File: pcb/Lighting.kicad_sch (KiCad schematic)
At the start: 5 parts, among them U4 TXS0101DBV

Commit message: First pass of applying footprints to most components.
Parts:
- JP10: footprint (none) -> Jumper:SolderJumper-2_P1.3mm_Bridged_RoundedPad1.0x1.5mm
- JP11: footprint (none) -> Jumper:SolderJumper-2_P1.3mm_Open_TrianglePad1.0x1.5mm
- R8: footprint (none) -> Resistor_SMD:R_0603_1608Metric_Pad0.98x0.95mm_HandSolder
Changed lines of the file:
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@@
 			)
 		)
-		(property "Footprint" ""
+		(property "Footprint" "Jumper:SolderJumper-2_P1.3mm_Open_TrianglePad1.0x1.5mm"
 			(at 101.6 49.53 0)
 			(effects
@@
 			)
 		)
-		(property "Footprint" ""
+		(property "Footprint" "Jumper:SolderJumper-2_P1.3mm_Bridged_RoundedPad1.0x1.5mm"
 			(at 88.9 77.47 0)
 			(effects
@@
 			)
 		)
-		(property "Footprint" ""
+		(property "Footprint" "Resistor_SMD:R_0603_1608Metric_Pad0.98x0.95mm_HandSolder"
 			(at 88.9 47.752 90)
 			(effects

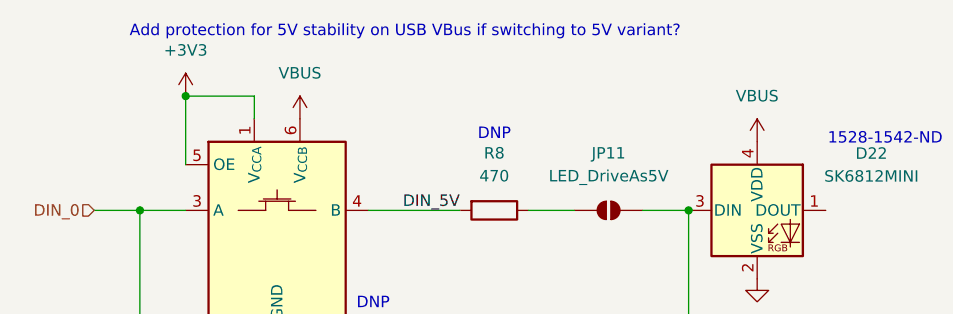
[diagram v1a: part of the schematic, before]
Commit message: Switching from a full USB protection chip for OVP and ESD, needed for USB PD to only ESD protection. Also added chips for ESD protection for the Ethernet connectors to the other hand.
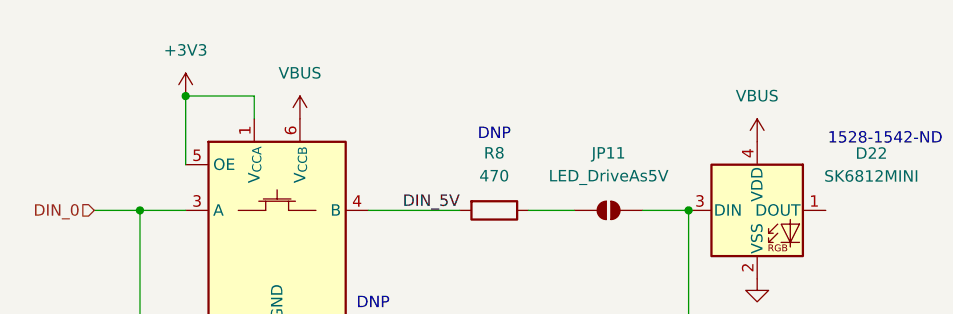
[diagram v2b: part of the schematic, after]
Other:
- note removed: "Add protection for 5V stability on USB VBus if switching to 5V variant?"
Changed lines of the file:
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@@
-		)
-	)
-	(text "Add protection for 5V stability on USB VBus if switching to 5V variant?"
-		(exclude_from_sim no)
-		(at 78.994 29.718 0)
-		(effects
-			(font
-				(size 1.27 1.27)
-			)
 		)
 	)

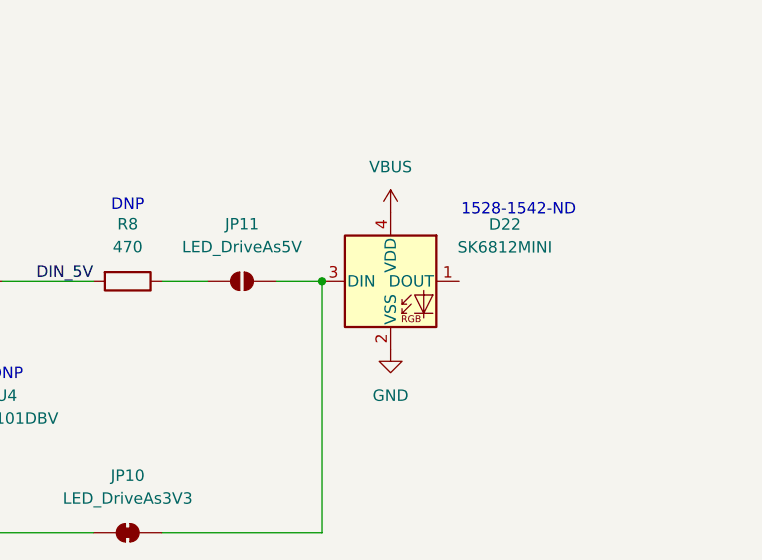
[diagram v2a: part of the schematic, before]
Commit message: Adding jumpers to test/swap between powering SK6812 with 3.3V or 5V.
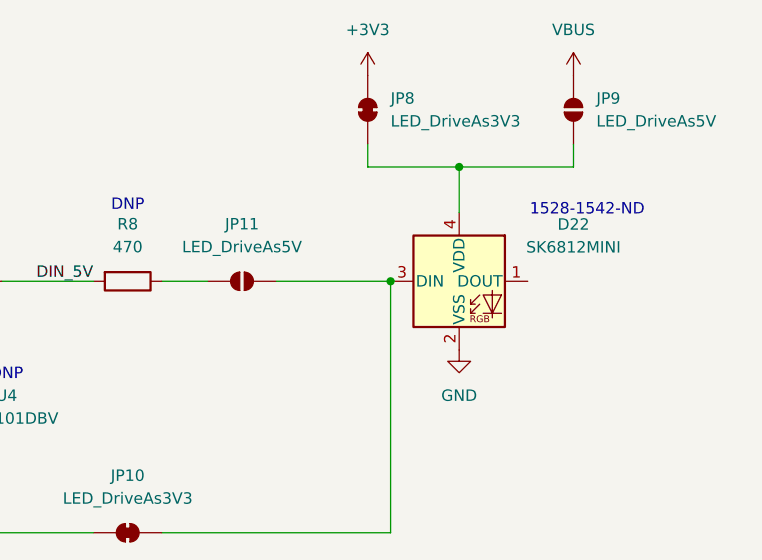
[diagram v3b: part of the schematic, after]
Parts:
- added JP8: LED_DriveAs3V3, Jumper:SolderJumper-2_P1.3mm_Bridged_RoundedPad1.0x1.5mm, symbol Jumper:SolderJumper_2_Bridged
- added JP9: LED_DriveAs5V, Jumper:SolderJumper-2_P1.3mm_Open_TrianglePad1.0x1.5mm, symbol Jumper:SolderJumper_2_Open
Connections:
- net +3V3: now also JP8.2 (B)
- net VBUS: now also JP9.2 (B); no longer D22.4 (VDD)
- new net: D22.4 (VDD), JP8.1 (A), JP9.1 (A)
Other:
- moved on the sheet: D22

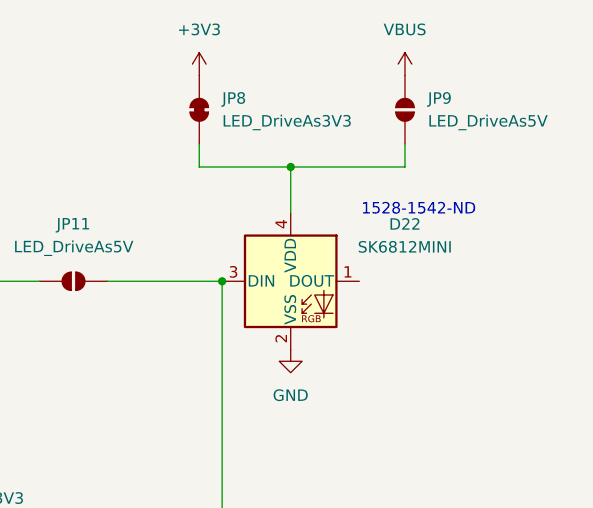
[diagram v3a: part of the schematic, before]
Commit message: Starting to position components and flipping passives as needed. Looking like board size is likely to need to be expanded.
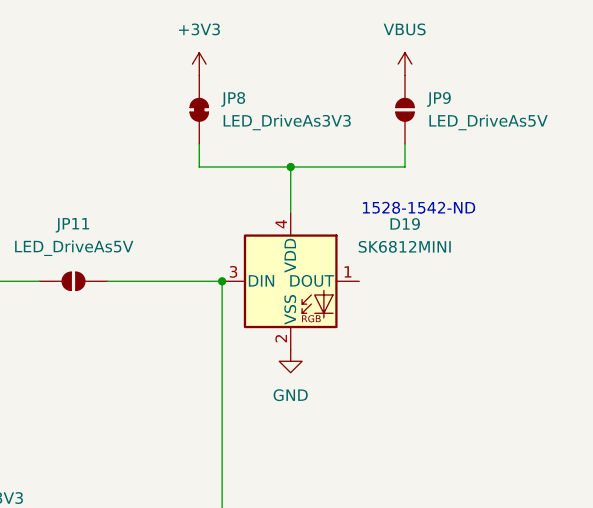
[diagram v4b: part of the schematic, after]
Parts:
- renumbered D22 to D19
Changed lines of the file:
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@@
 		(dnp no)
 		(fields_autoplaced yes)
-		(property "Reference" "D22"
+		(property "Reference" "D19"
 			(at 138.43 43.2114 0)
 			(effects
@@
 			(project "cheapino"
 				(path "/9203b006-47ac-4f34-8cc4-2b709e3df56f/23d46689-c88a-4d8a-9ead-5dd5573c8b8b"
-					(reference "D22")
+					(reference "D19")
 					(unit 1)
 				)

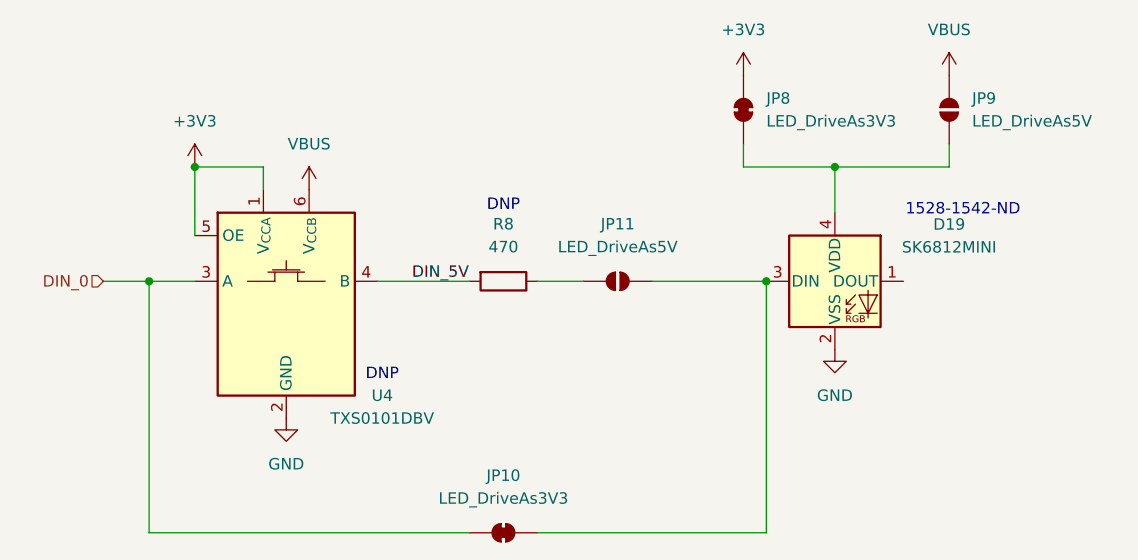
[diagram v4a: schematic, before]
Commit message: WIP: Starting to migrate toward 2 independant halves.
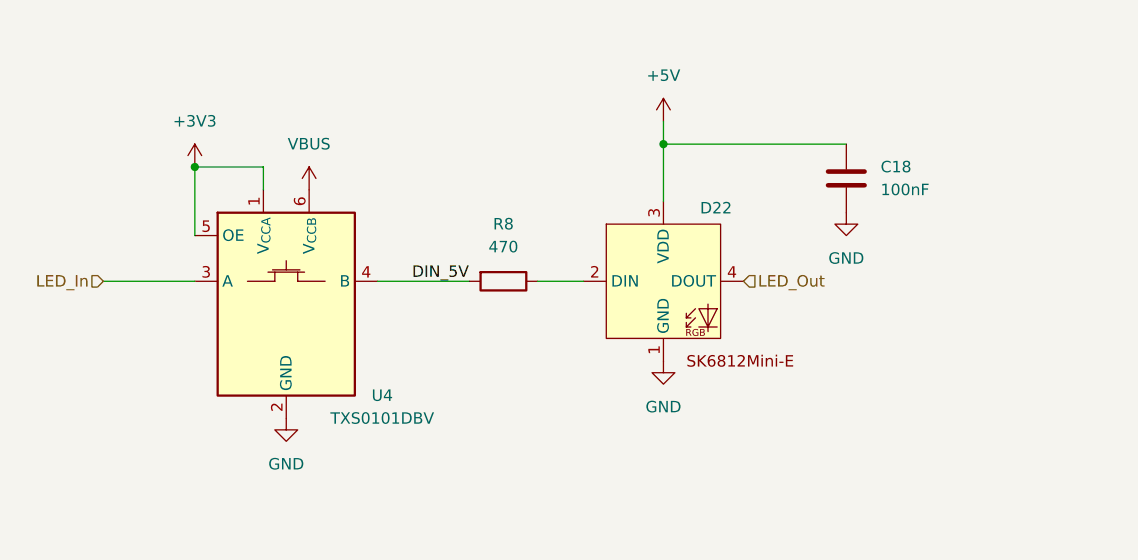
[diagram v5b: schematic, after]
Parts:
- removed D19: SK6812MINI, LED_SMD:LED_SK6812MINI_PLCC4_3.5x3.5mm_P1.75mm, symbol LED:SK6812MINI
- removed JP10, JP8: LED_DriveAs3V3, Jumper:SolderJumper-2_P1.3mm_Bridged_RoundedPad1.0x1.5mm, symbol Jumper:SolderJumper_2_Bridged
- removed JP11, JP9: LED_DriveAs5V, Jumper:SolderJumper-2_P1.3mm_Open_TrianglePad1.0x1.5mm, symbol Jumper:SolderJumper_2_Open
- added C18: 100nF, Capacitor_SMD:C_0805_2012Metric_Pad1.18x1.45mm_HandSolder, symbol Device:C
- added D22: ~, Extra:SK6812-MINI-E_ReverseMount, symbol Extra:SK6812Mini-E
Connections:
- net GND: now also C18.2, D22.1 (GND)
- net at R8.1: now also D22.2 (DIN)
- net DIN_0 renamed LED_In
- new net +5V: C18.1, D22.3 (VDD)
- new net LED_Out: D22.4 (DOUT)
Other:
- note removed: "1528-1542-ND"
- note removed: "DNP"

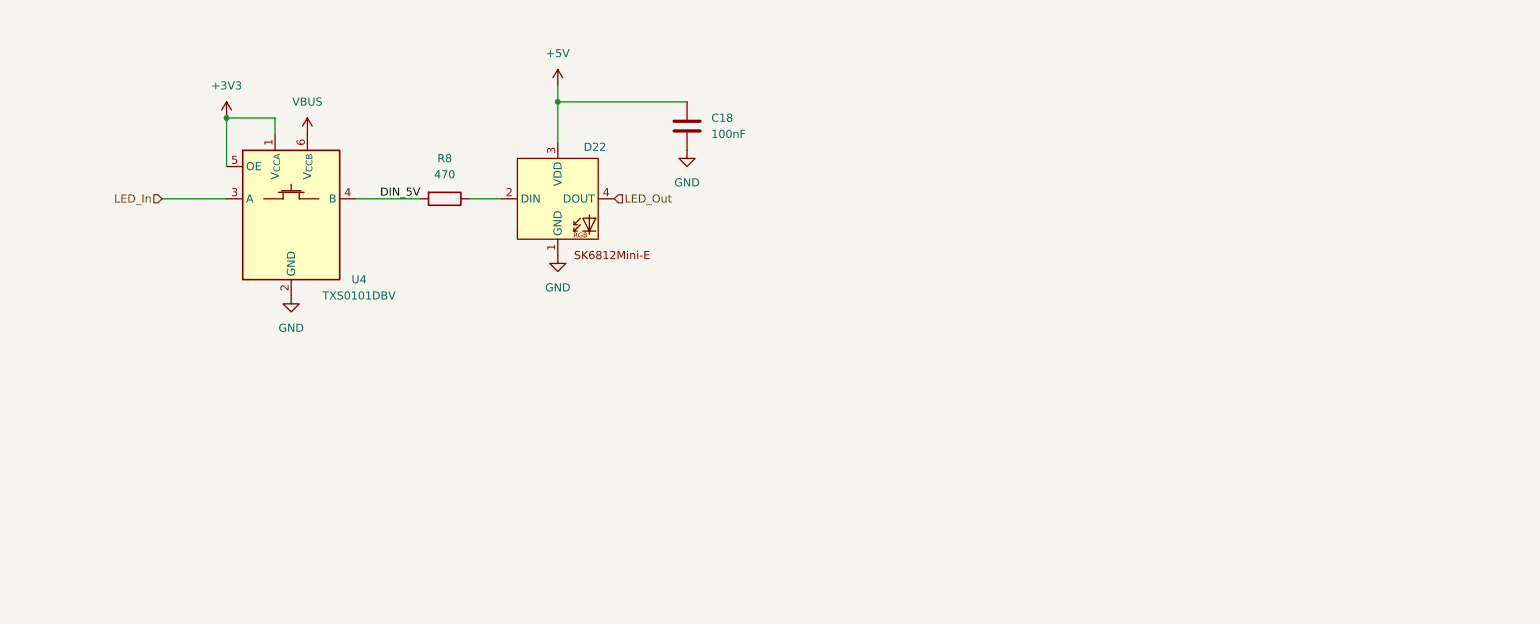
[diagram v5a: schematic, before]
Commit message: WIP: Updating keyboard matrix to use the new shared part and reorganizing all the LED outputs.
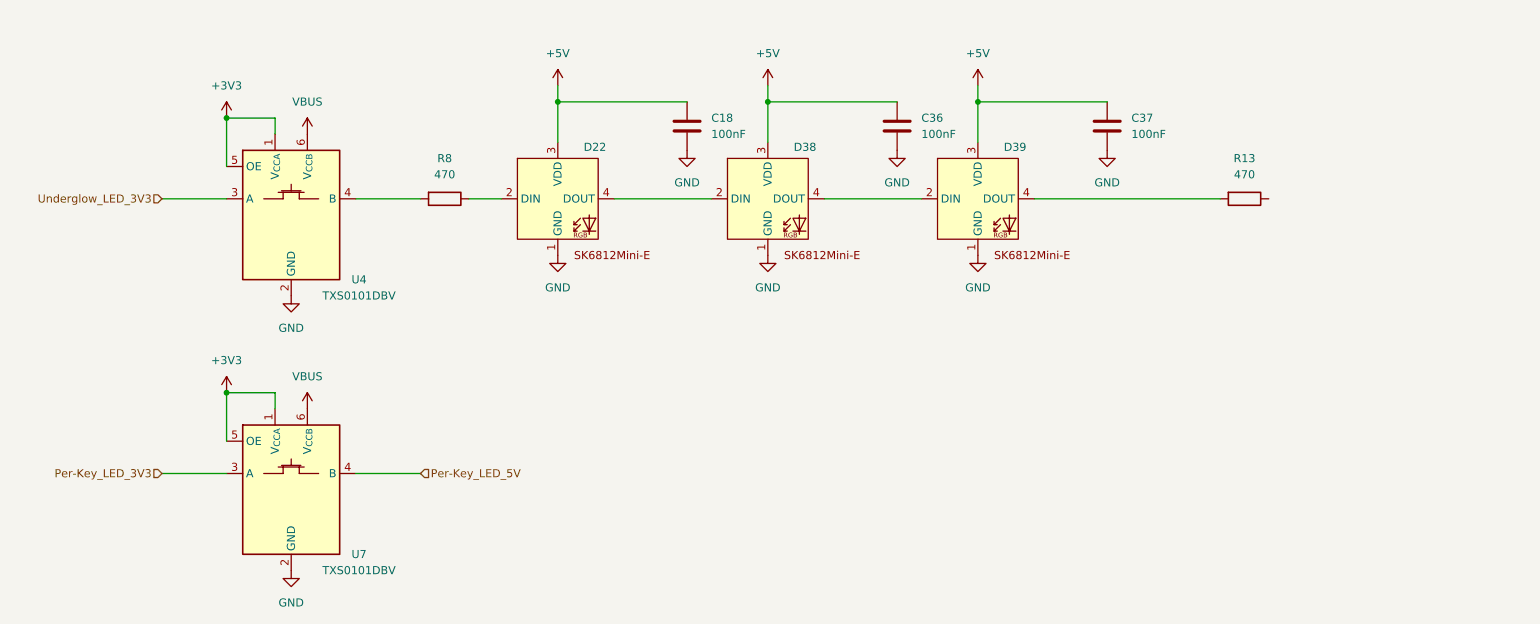
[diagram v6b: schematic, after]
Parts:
- added C36, C37: 100nF, Capacitor_SMD:C_0603_1608Metric_Pad1.08x0.95mm_HandSolder, symbol Device:C
- added D38, D39: ~, Extra:SK6812-MINI-E_ReverseMount, symbol Extra:SK6812Mini-E
- added R13: 470, Resistor_SMD:R_0603_1608Metric_Pad0.98x0.95mm_HandSolder, symbol Device:R
- added U7: TXS0101DBV, Package_TO_SOT_SMD:SOT-23-6, symbol Logic_LevelTranslator:TXS0101DBV
- C18: footprint Capacitor_SMD:C_0805_2012Metric_Pad1.18x1.45mm_HandSolder -> Capacitor_SMD:C_0603_1608Metric_Pad1.08x0.95mm_HandSolder
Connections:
- net +3V3: now also U7.1 (V_{CCA}), U7.5 (OE)
- net +5V: now also C36.1, C37.1, D38.3 (VDD), D39.3 (VDD)
- net GND: now also C36.2, C37.2, D38.1 (GND), D39.1 (GND), U7.2 (GND)
- net VBUS: now also U7.6 (V_{CCB})
- net DIN_5V: no longer names the net of R8.2, U4.4 (B)
- net LED_In renamed Underglow_LED_3V3
- net LED_Out: no longer names the net of D22.4 (DOUT)
- net LED_Out: now also D38.2 (DIN)
- new net: D39.4 (DOUT), R13.2
- new net: D38.4 (DOUT), D39.2 (DIN)
- new net Per-Key_LED_3V3: U7.3 (A)
- new net Per-Key_LED_5V: U7.4 (B)

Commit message: Adding reversible MX Sockets and SK6812MiniE footprints, finishing the replacement of Ethernet with a TRRS connector and selectable 0Ohm resistors to swap Rx/Tx for the interconnect.
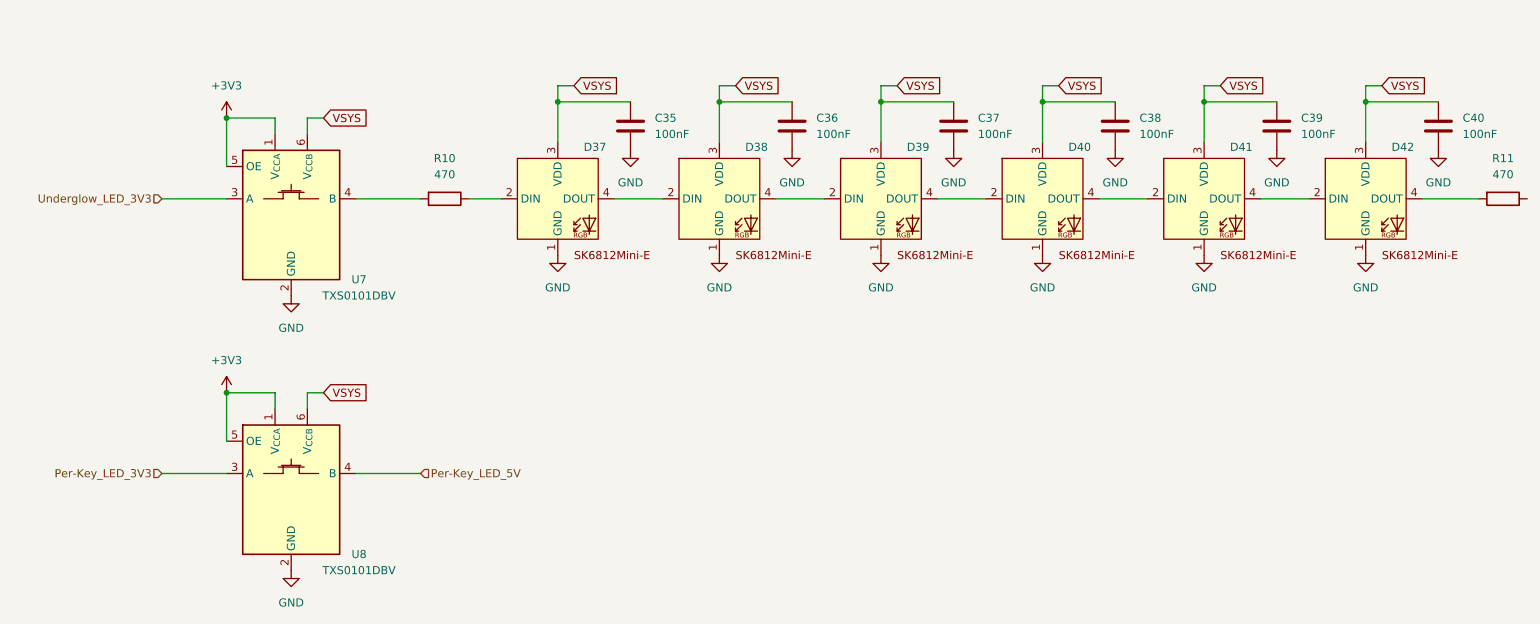
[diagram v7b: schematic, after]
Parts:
- added C38, C39, C40: 100nF, Capacitor_SMD:C_0603_1608Metric_Pad1.08x0.95mm_HandSolder, symbol Device:C
- added D40, D41, D42: ~, Extra:SK6812-MINI-E_ReverseMount_reversible, symbol Extra:SK6812Mini-E
- D37: renamed from D22; footprint Extra:SK6812-MINI-E_ReverseMount -> Extra:SK6812-MINI-E_ReverseMount_reversible
- D38, D39: footprint Extra:SK6812-MINI-E_ReverseMount -> Extra:SK6812-MINI-E_ReverseMount_reversible
- R10: renamed from R8; footprint Resistor_SMD:R_0603_1608Metric_Pad0.98x0.95mm_HandSolder -> Resistor_SMD:R_0805_2012Metric_Pad1.20x1.40mm_HandSolder
- R11: renamed from R13; footprint Resistor_SMD:R_0603_1608Metric_Pad0.98x0.95mm_HandSolder -> Resistor_SMD:R_0805_2012Metric_Pad1.20x1.40mm_HandSolder
- renumbered C18 to C35, U4 to U7, U7 to U8
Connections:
- net VBUS is gone; now on net VSYS: U7.6 (V_{CCB}), U8.6 (V_{CCB})
- net GND: now also C38.2, C39.2, C40.2, D40.1 (GND), D41.1 (GND), D42.1 (GND)
- net at D39.4 (DOUT): now also D40.2 (DIN); no longer R11.2
- net +5V renamed VSYS
- net VSYS: now also C38.1, C39.1, C40.1, D40.3 (VDD), D41.3 (VDD), D42.3 (VDD)
- new net: D40.4 (DOUT), D41.2 (DIN)
- new net: D42.4 (DOUT), R11.2
- new net: D41.4 (DOUT), D42.2 (DIN)
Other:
- moved on the sheet: C35, C36, C37, D38, D39, R11

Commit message: Broke out Underglow LEDs into a common hierarchical sheet for what may be more consistent placements. Additionally created hierarchical PCB layouts and started using the HierarchicalPcb plugin (https://github.com/gauravmm/HierarchicalPcb.git) to automatically layout repeated components for the keymap.
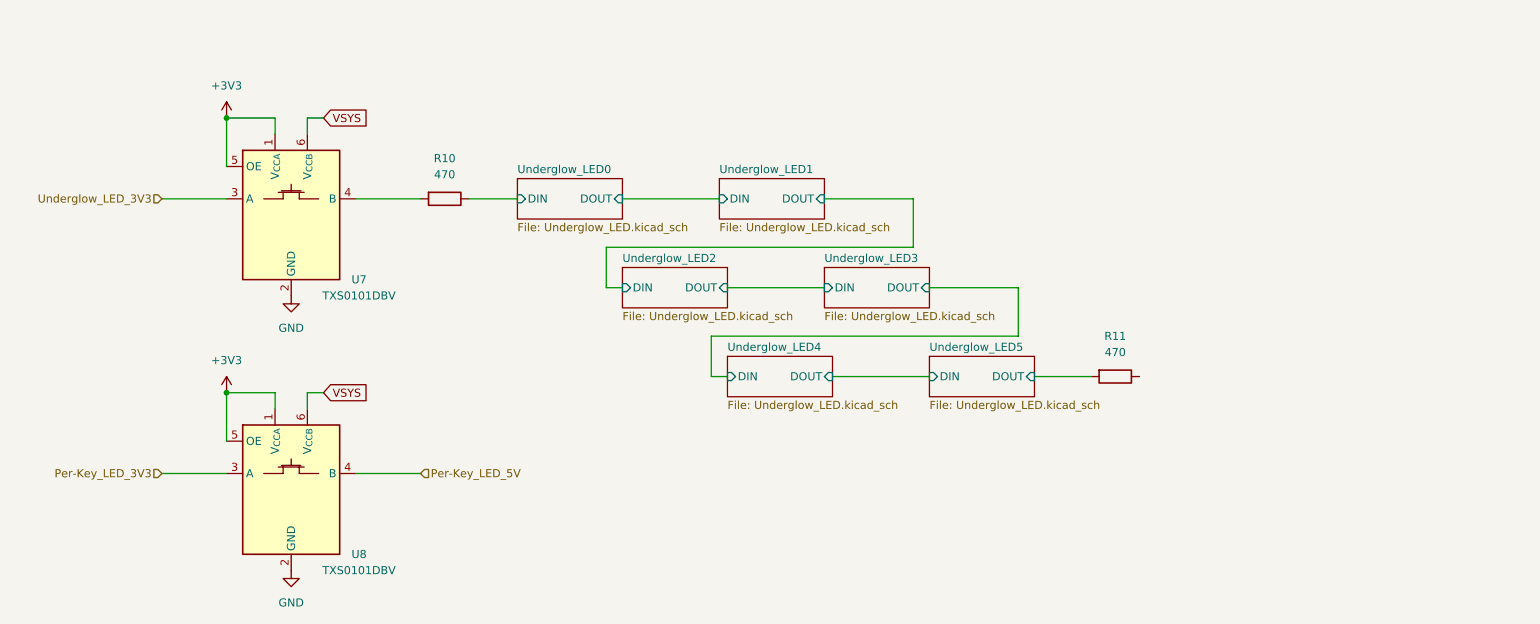
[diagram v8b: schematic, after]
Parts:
- removed C35, C36, C37, C38, C39, C40: 100nF, Capacitor_SMD:C_0603_1608Metric_Pad1.08x0.95mm_HandSolder, symbol Device:C
- removed D37, D38, D39, D40, D41, D42: ~, Extra:SK6812-MINI-E_ReverseMount_reversible, symbol Extra:SK6812Mini-E
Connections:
- net Underglow_LED0/DIN: now reaches R10.1
- net Underglow_LED5/DOUT: now reaches R11.2
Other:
- added sheet Underglow_LED0 (Underglow_LED.kicad_sch)
- added sheet Underglow_LED1 (Underglow_LED.kicad_sch)
- added sheet Underglow_LED2 (Underglow_LED.kicad_sch)
- added sheet Underglow_LED3 (Underglow_LED.kicad_sch)
- added sheet Underglow_LED4 (Underglow_LED.kicad_sch)
- added sheet Underglow_LED5 (Underglow_LED.kicad_sch)
- moved on the sheet: R11
